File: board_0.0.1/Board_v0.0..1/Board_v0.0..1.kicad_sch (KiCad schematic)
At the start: 2 parts, among them J1 178780-9, U1 Teensy3.5

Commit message: update
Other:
- added sheet Power (power.kicad_sch)
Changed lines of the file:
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@@
+		)
+	)
+	(sheet
+		(at 31.75 172.72)
+		(size 17.78 17.78)
+		(fields_autoplaced yes)
+		(stroke
+			(width 0.1524)
+			(type solid)
+		)
+		(fill
+			(color 0 0 0 0.0000)
+		)
+		(property "Sheetname" "Power"
+			(at 31.75 172.0084 0)
+			(effects
+				(font
+					(size 1.27 1.27)
+				)
+				(justify left bottom)
+			)
+		)
+		(property "Sheetfile" "power.kicad_sch"
+			(at 31.75 191.0846 0)
+			(effects
+				(font
+					(size 1.27 1.27)
+				)
+				(justify left top)
+			)
+		)
+		(instances
+			(project "Board_v0.0..1"
+				(path "/84a654bf-6339-4456-82e8-fc3535e299fc"
+					(page "2")
+				)
+			)
 		)
 	)

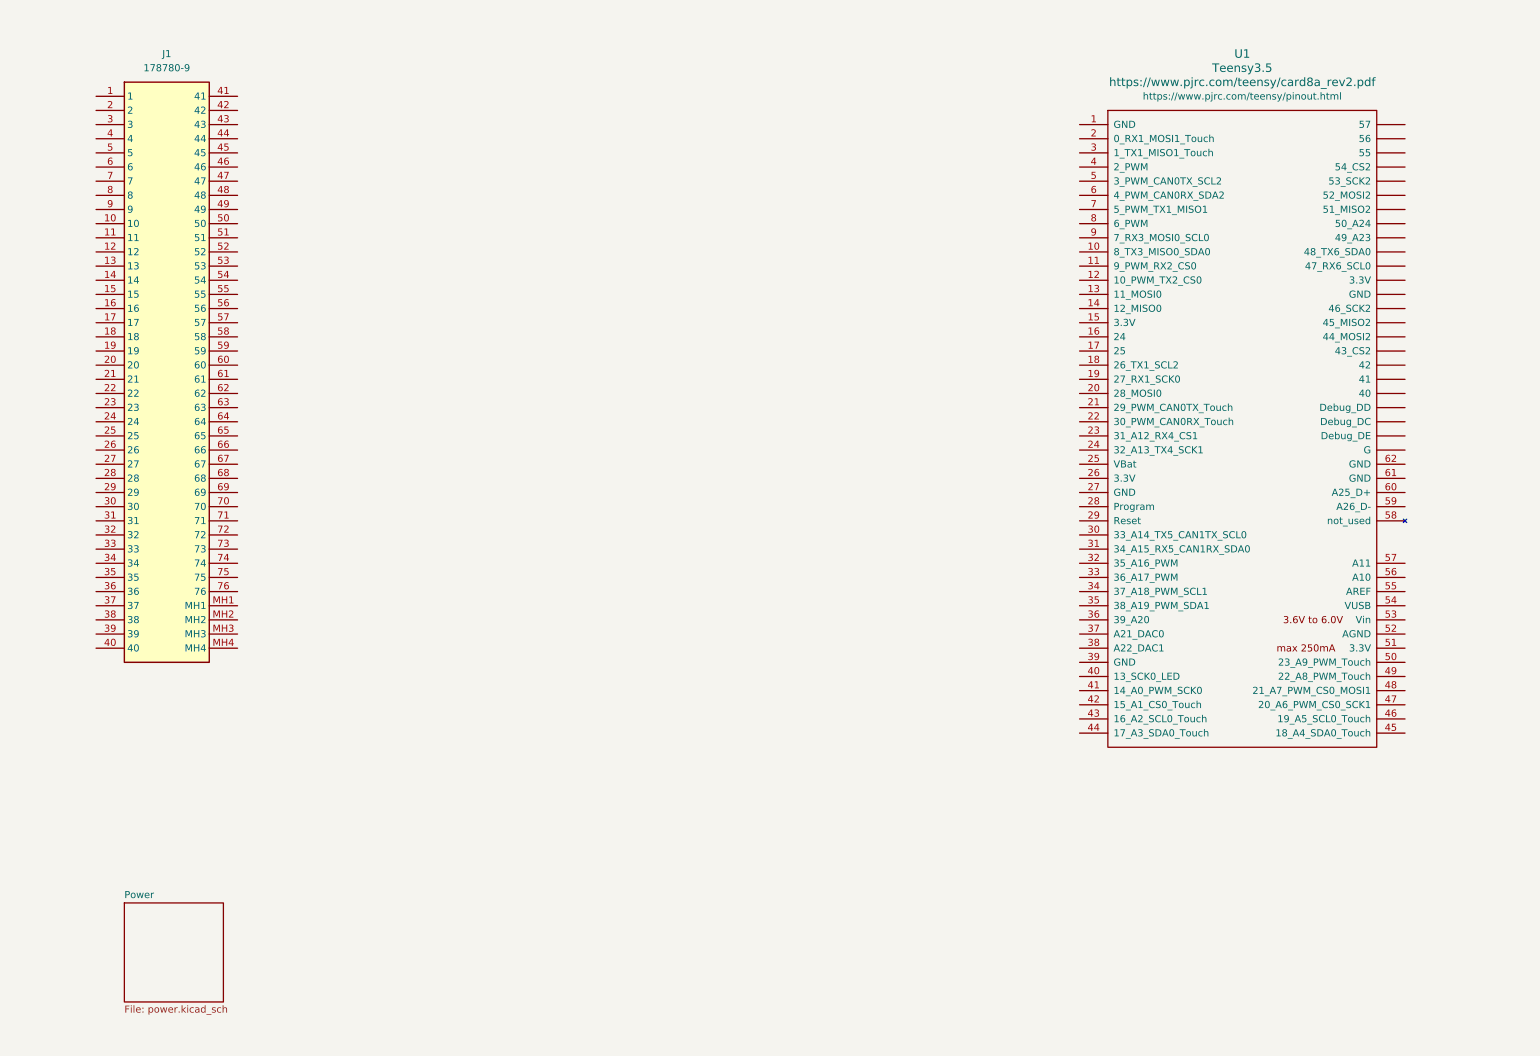
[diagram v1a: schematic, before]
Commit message: added vr conditioner from speeduino
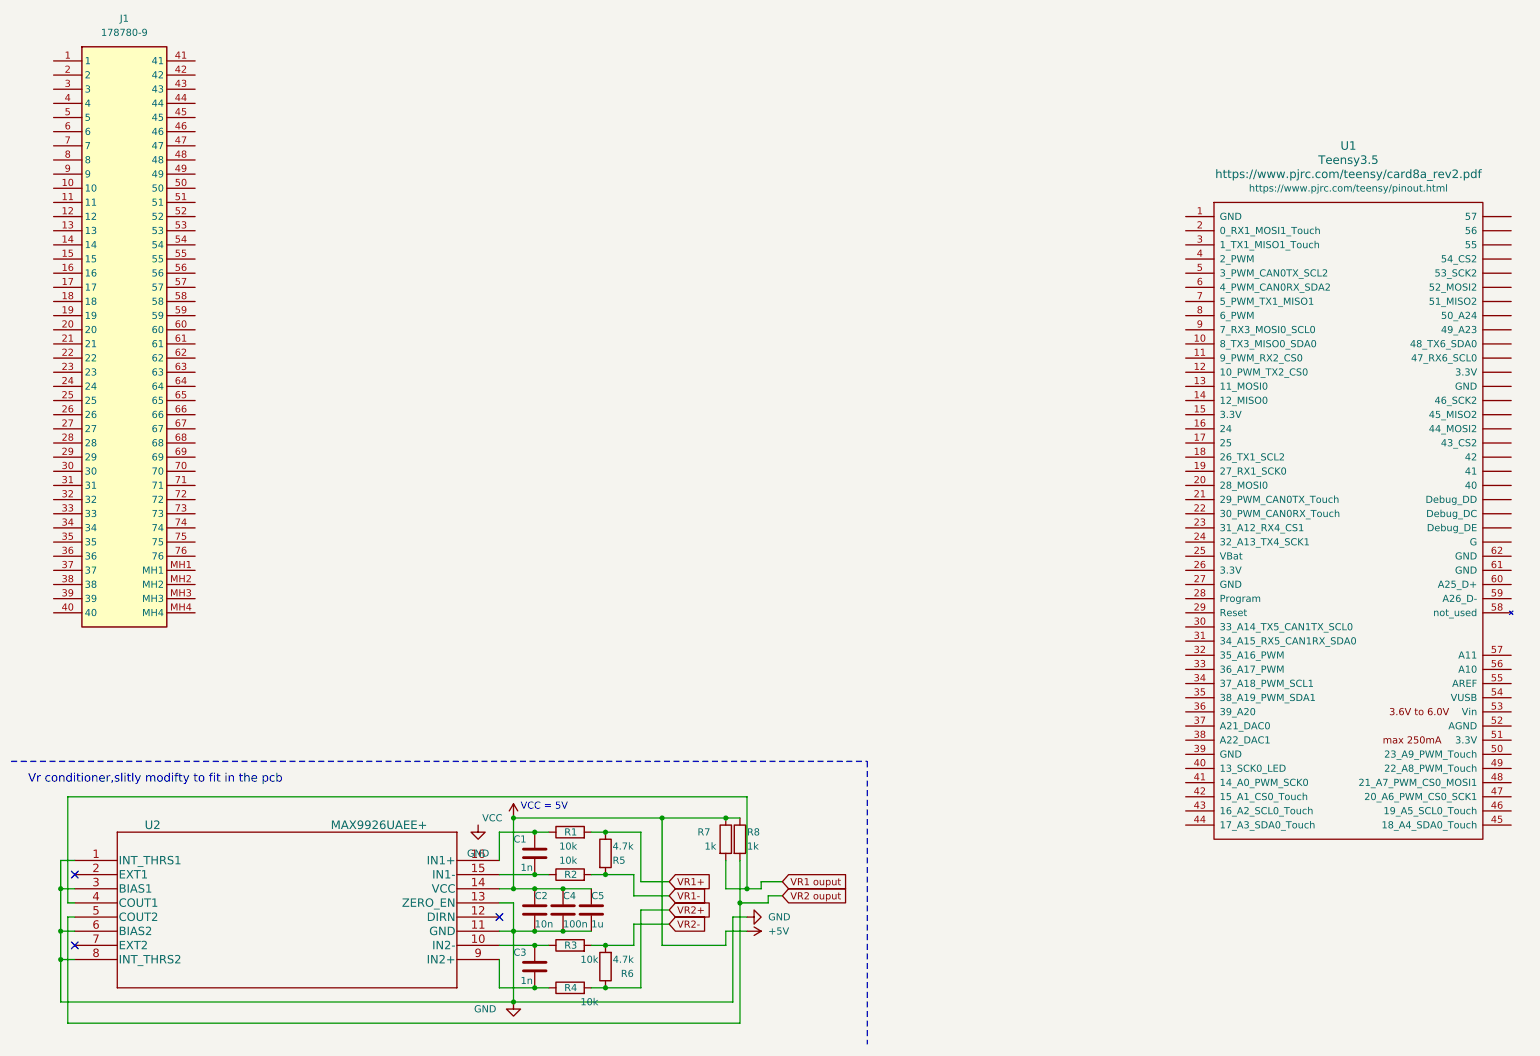
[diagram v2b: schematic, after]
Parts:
- added C1, C3: 1n, Capacitor_SMD:C_0603_1608Metric, symbol Device:C
- added C2: 10n, Capacitor_SMD:C_0603_1608Metric, symbol Device:C
- added C4: 100n, Capacitor_SMD:C_0603_1608Metric, symbol Device:C
- added C5: 1u, Capacitor_SMD:C_0603_1608Metric, symbol Device:C
- added R1, R2, R3, R4: 10k, Resistor_SMD:R_1206_3216Metric, symbol Device:R
- added R5, R6: 4.7k, Resistor_THT:R_Axial_DIN0207_L6.3mm_D2.5mm_P7.62mm_Horizontal, symbol Device:R
- added R7, R8: 1k, Resistor_SMD:R_0603_1608Metric_Pad1.05x0.95mm_HandSolder, symbol Device:R
- added U2: MAX9926UAEE+, MAX9926UAEE+:MAX9926UAEE&plus_, symbol 2021-02-17_17-37-40:MAX9926UAEE+
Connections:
- new net: C3.1, R3.1, U2.10 (IN2-)
- new net: C3.2, R4.1, U2.9 (IN2+)
- new net: C1.2, R2.1, U2.15 (IN1-)
- new net: C1.1, R1.1, U2.16 (IN1+)
- new net +5V: C2.1, C4.1, C5.1, R7.1, R8.1, U2.14 (VCC)
- new net GND: C2.2, C4.2, C5.2, U2.1 (INT_THRS1), U2.11 (GND), U2.13 (ZERO_EN), U2.3 (BIAS1), U2.6 (BIAS2), U2.8 (INT_THRS2)
- new net VR1 ouput: R7.2, U2.4 (COUT1)
- new net VR1+: R1.2, R5.1
- new net VR1-: R2.2, R5.2
- new net VR2 ouput: R8.2, U2.5 (COUT2)
- new net VR2+: R4.2, R6.1
- new net VR2-: R3.2, R6.2
- no-connect marks 0 -> 3
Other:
- removed sheet Power
- note added: "VCC = 5V"
- note added: "Vr conditioner,slitly modifty to fit in the pcb"
- moved on the sheet: J1, U1
